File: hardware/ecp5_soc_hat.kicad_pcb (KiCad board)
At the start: 2 copper layers, 67 x 84 mm, 31 parts, among them J1 DB15_Female_HighDensity_Mount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, J2 USB_A, U1 AS4C32M16SB, U2 74HC240, U3 LM2731XMF, X1 XO32, X3 HDR40, X4 HDR40

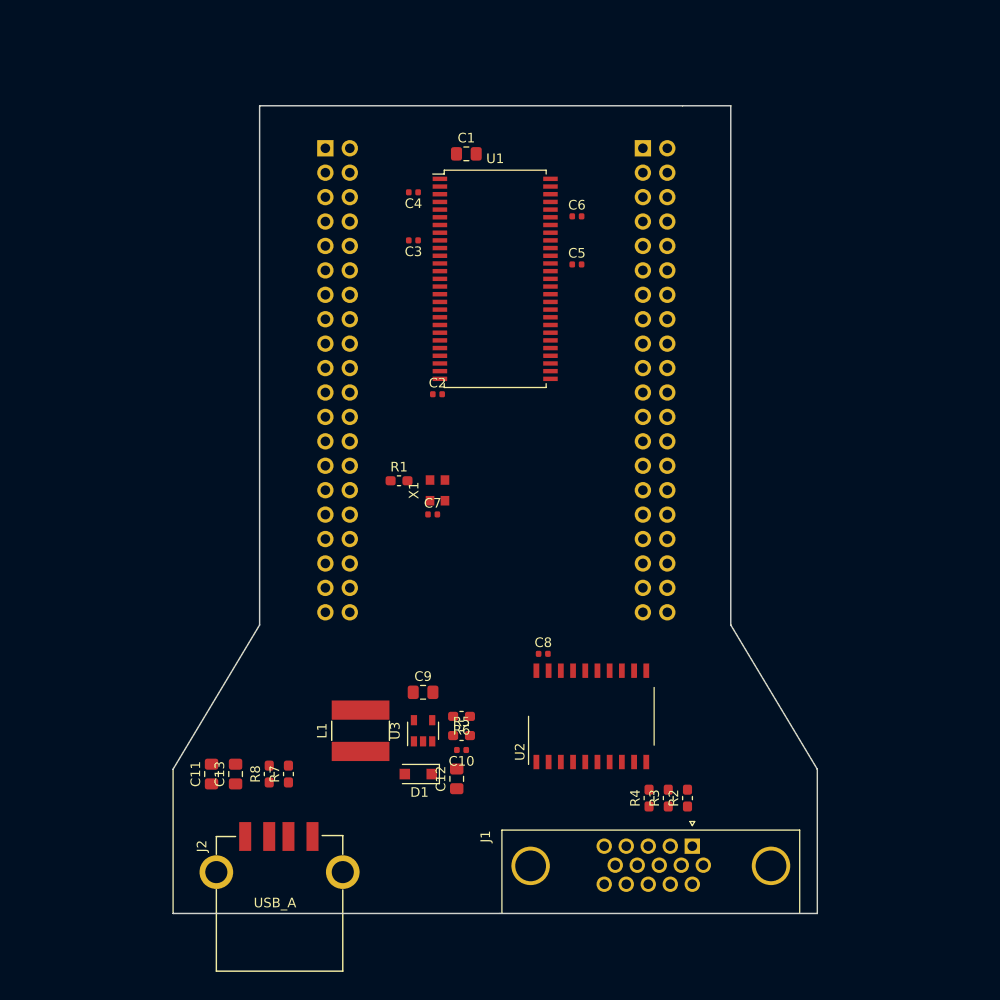
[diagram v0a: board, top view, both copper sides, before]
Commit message: PCB fully routed
Signed-off-by: David Shah <davey1576@gmail.com>
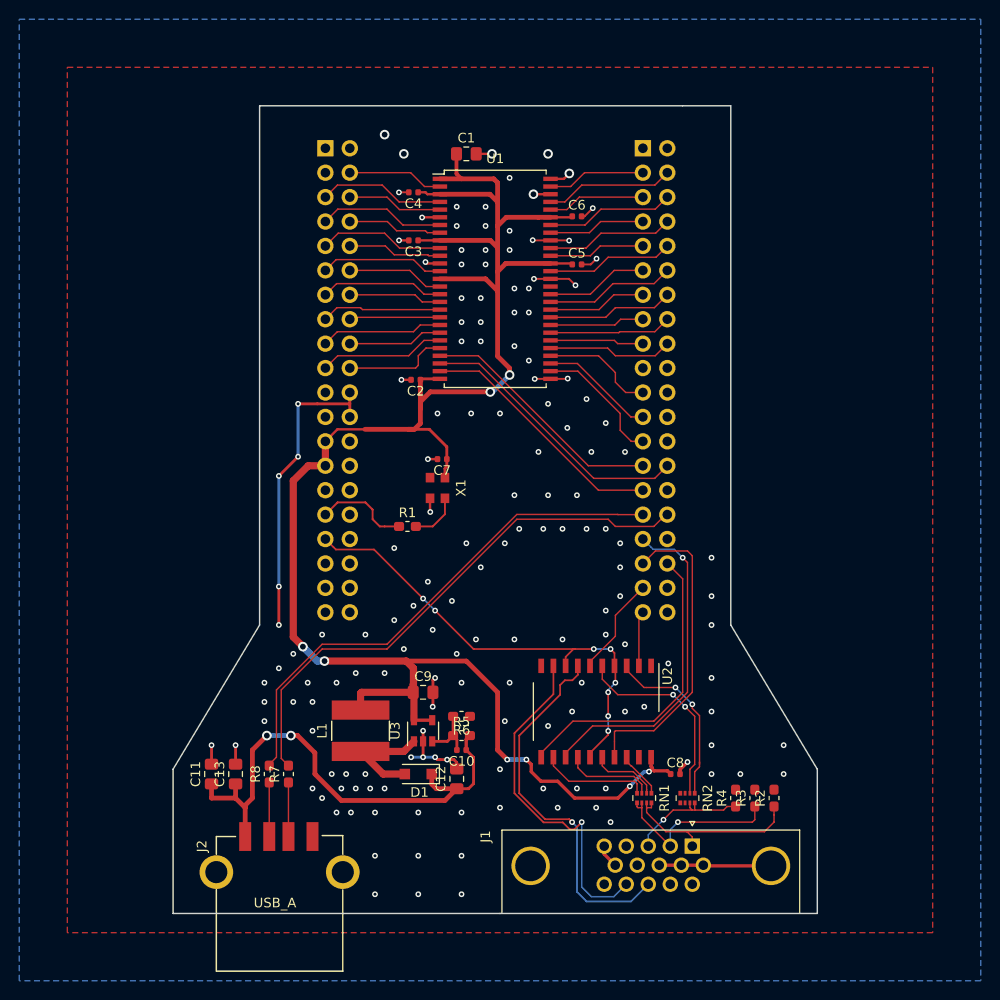
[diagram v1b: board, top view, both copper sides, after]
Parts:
- added RN1: R_Pack04, Resistor_SMD:R_Array_Convex_4x0402, F.Cu at (150.0, 126.0)
- added RN2: R_Pack04, Resistor_SMD:R_Array_Convex_4x0402, F.Cu at (154.5, 126.0)
- R2, R3, R4: value 270 -> DNP
- U2: value 74HC240 -> 74HC244
- moved C8 18.6 mm to (153.2, 123.5)
- moved R2 9.00 mm to (163.5, 126.0)
- moved R3 9.00 mm to (161.5, 126.0)
- moved R4 9.00 mm to (159.5, 126.0)
- moved C7 5.83 mm to (129.0, 90.8), turned to 180 degrees
- moved R1 4.83 mm to (125.4, 97.8)
- moved C2 2.72 mm to (126.2, 82.5), turned to 180 degrees
- moved U2 0.71 mm to (145.0, 117.0), turned to 270 degrees
- moved X1 0.25 mm to (128.5, 93.8), turned to 270 degrees
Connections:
- net Net-(J1-Pad1) renamed /VGA_VR
- net Net-(J1-Pad2) renamed /VGA_VG
- net Net-(J1-Pad3) renamed /VGA_VB
- J1 pad 13: Net-(J1-Pad13) -> /HS_BUF
- J1 pad 14: Net-(J1-Pad14) -> /VS_BUF
- R2 pad 2: Net-(R2-Pad2) -> GND
- R3 pad 2: Net-(R3-Pad2) -> GND
- R4 pad 2: Net-(R4-Pad2) -> GND
- U2 pad 11: GND -> /VGA_VS
- U2 pad 12: Net-(J1-Pad13) -> Net-(RN1-Pad4)
- U2 pad 13: GND -> /VGA_HS
- U2 pad 14: Net-(R4-Pad2) -> Net-(RN1-Pad3)
- U2 pad 15: GND -> /VGA_BRIGHT
- U2 pad 16: Net-(R3-Pad2) -> Net-(RN1-Pad2)
- U2 pad 17: /VGA_VS -> /VGA_B
- U2 pad 18: Net-(R2-Pad2) -> Net-(RN1-Pad1)
- U2 pad 3: Net-(J1-Pad14) -> Net-(RN2-Pad1)
- U2 pad 4: /VGA_G -> /VGA_BRIGHT
- U2 pad 6: /VGA_B -> /VGA_G
- U2 pad 7: Net-(U2-Pad7) -> /HS_BUF
- U2 pad 8: /VGA_HS -> /VGA_BRIGHT
- U2 pad 9: Net-(U2-Pad9) -> /VS_BUF
- X3 pad 10: /RAM_A11 -> /RAM_DQ6
- X3 pad 11: /RAM_A3 -> /RAM_DQ7
- X3 pad 12: /RAM_A12 -> /RAM_DQM0
- X3 pad 13: /RAM_A4 -> /RAM_~WE
- X3 pad 14: /RAM_BA0 -> /RAM_~CAS
- X3 pad 15: /RAM_A5 -> /RAM_~RAS
- X3 pad 16: /RAM_BA1 -> /RAM_~CS
- X3 pad 17: /RAM_A6 -> /RAM_BA0
- X3 pad 18: /RAM_~WE -> /RAM_BA1
- X3 pad 19: /RAM_A7 -> /RAM_A10
- X3 pad 20: /RAM_~CS -> /RAM_A0
- X3 pad 33: /EXPCON_CLKOUT -> /VGA_BRIGHT
- X3 pad 4: /RAM_A8 -> /RAM_DQ0
- X3 pad 5: /RAM_A0 -> /RAM_DQ1
- X3 pad 6: /RAM_A9 -> /RAM_DQ2
- X3 pad 7: /RAM_A1 -> /RAM_DQ3
- X3 pad 8: /RAM_A10 -> /RAM_DQ4
- X3 pad 9: /RAM_A2 -> /RAM_DQ5
- X4 pad 10: /RAM_DQ11 -> /RAM_DQ8
- X4 pad 11: /RAM_DQM0 -> /RAM_DQM1
- X4 pad 12: /RAM_DQ12 -> /RAM_CLK
- X4 pad 13: /RAM_DQM1 -> /RAM_CKE
- X4 pad 14: /RAM_DQ13 -> /RAM_A12
- X4 pad 15: /RAM_DQ0 -> /RAM_A11
- X4 pad 16: /RAM_DQ14 -> /RAM_A9
- X4 pad 17: /RAM_DQ1 -> /RAM_A8
- X4 pad 18: /RAM_DQ15 -> /RAM_A7
- X4 pad 21: /RAM_DQ2 -> /RAM_A6
- X4 pad 23: /RAM_DQ3 -> /RAM_A5
- X4 pad 25: /RAM_DQ4 -> /RAM_A4
- X4 pad 27: /RAM_DQ5 -> /RAM_A1
- X4 pad 28: /USB_DP -> /RAM_A2
- X4 pad 29: /RAM_DQ6 -> /RAM_A3
- X4 pad 3: /RAM_~RAS -> /RAM_DQ15
- X4 pad 31: /RAM_DQ7 -> /USB_DM
- X4 pad 32: /USB_DM -> /USB_DP
- X4 pad 33: /VGA_R -> /VGA_HS
- X4 pad 35: /VGA_G -> /VGA_B
- X4 pad 37: /VGA_B -> /VGA_G
- X4 pad 39: /VGA_HS -> /VGA_R
- X4 pad 4: /RAM_DQ8 -> /RAM_DQ14
- X4 pad 5: /RAM_~CAS -> /RAM_DQ13
- X4 pad 6: /RAM_DQ9 -> /RAM_DQ12
- X4 pad 7: /RAM_CLK -> /RAM_DQ11
- X4 pad 9: /RAM_CKE -> /RAM_DQ9
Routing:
- net +3V3: track 0.00 -> 197.1 mm, vias 0 -> 8
- net GND: track 0.00 -> 92.6 mm, vias 0 -> 158
- net /USB_DP: track 0.00 -> 56.5 mm
- net +5V: track 0.00 -> 53.9 mm, vias 0 -> 2
- net /USB_DM: track 0.00 -> 53.9 mm
- net /VGA_BRIGHT: track 0.00 -> 49.1 mm, vias 0 -> 8
- net /HS_BUF: track 0.00 -> 39.0 mm, vias 0 -> 1
- net /VS_BUF: track 0.00 -> 36.1 mm, vias 0 -> 1
- net /VGA_HS: track 0.00 -> 34.9 mm, vias 0 -> 1
- net /VGA_B: track 0.00 -> 32.5 mm
- net /VGA_VS: track 0.00 -> 31.8 mm
- net /RAM_A2: track 0.00 -> 29.1 mm
- net /RAM_A3: track 0.00 -> 26.2 mm
- net /RAM_A1: track 0.00 -> 25.8 mm
- net Net-(RN2-Pad2): track 0.00 -> 20.8 mm, vias 0 -> 2
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- added copper zone on B.Cu, net GND
- added copper zone on F.Cu, net GND
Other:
- net class Default: clearance 0.2 -> 0.15; trace_width 0.25 -> 0.15; via_dia 0.8 -> 0.6; via_drill 0.4 -> 0.3
- rule trace_clearance: 0.2 -> 0.15
- rule trace_min: 0.2 -> 0.15
- rule via_min_size: 0.4 -> 0.6

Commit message: Tidy up board
Signed-off-by: David Shah <davey1576@gmail.com>
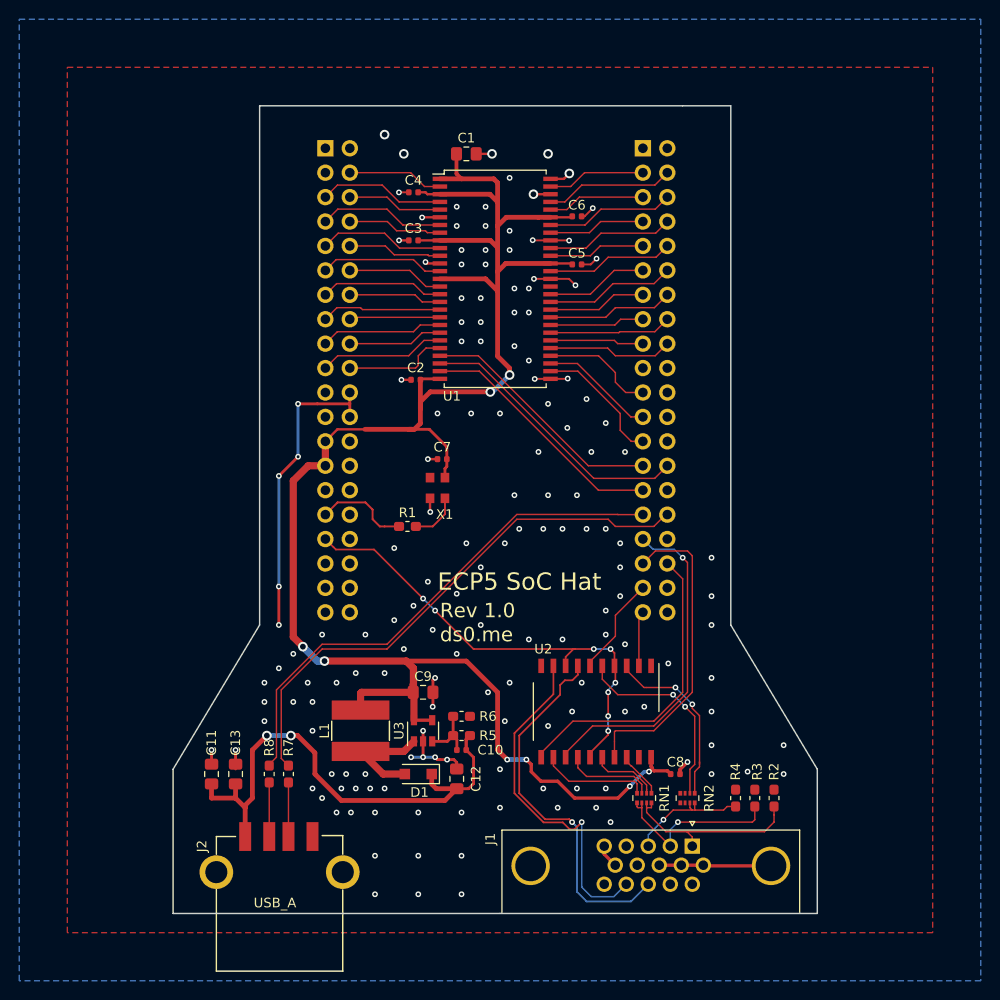
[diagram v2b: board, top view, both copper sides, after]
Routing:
- net GND: track 92.6 -> 92.1 mm
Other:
- board text added: "ECP5 SoC Hat"
- board text added: "Rev 1.0"
- board text added: "ds0.me"

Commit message: Production PCBs rev1.0
Signed-off-by: David Shah <davey1576@gmail.com>
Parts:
- added J3: Conn_02x04_Odd_Even, Connector_PinHeader_2.54mm:PinHeader_2x04_P2.54mm_Vertical, F.Cu at (136.0, 104.5)
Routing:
- net /VGA_HS: track 34.9 -> 50.0 mm
- net /VGA_VS: track 31.8 -> 46.5 mm
- net /VGA_B: track 32.5 -> 45.9 mm
- net /VGA_R: track 5.74 -> 17.1 mm, vias 0 -> 2
- net /VGA_BRIGHT: track 49.1 -> 58.5 mm
- net +3V3: track 197.1 -> 206.4 mm, vias 8 -> 10
- net /VGA_G: track 10.4 -> 14.9 mm
- net GND: vias 158 -> 157
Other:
- rule pad_to_mask_clearance: 0.2 -> 0
